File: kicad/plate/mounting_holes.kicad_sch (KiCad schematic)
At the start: 22 parts

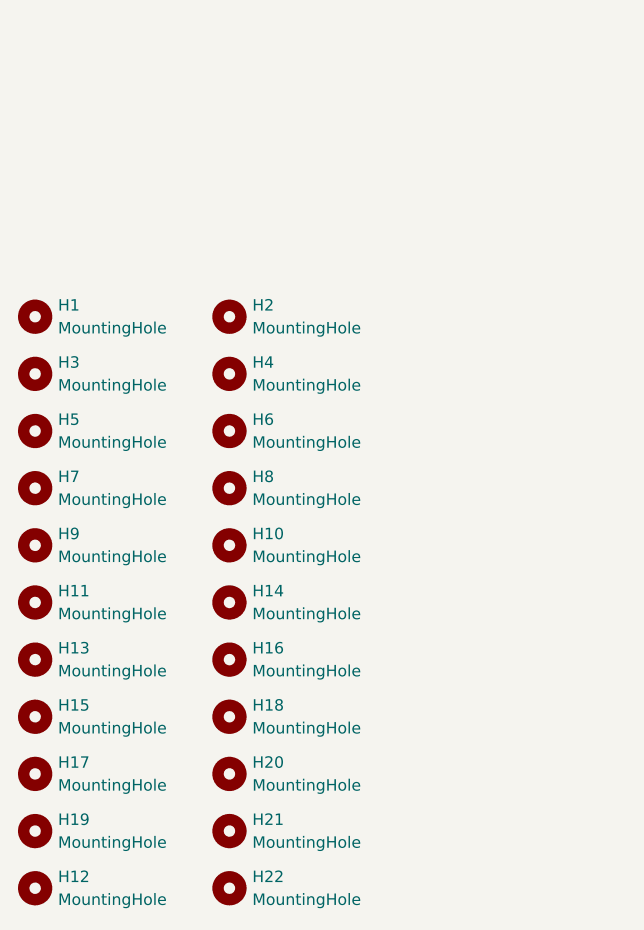
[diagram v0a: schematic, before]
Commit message: should be ok for proto order
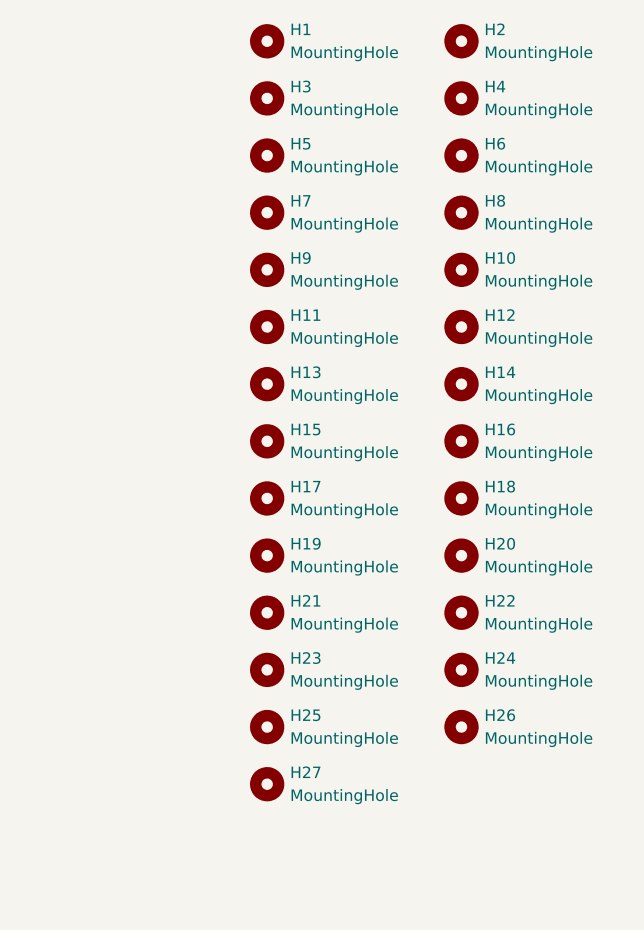
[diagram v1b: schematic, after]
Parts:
- added H23, H24, H25, H26, H27: MountingHole, MountingHole:MountingHole_2.2mm_M2_DIN965, symbol Mechanical:MountingHole
